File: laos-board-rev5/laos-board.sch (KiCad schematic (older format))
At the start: 98 parts, among them IC1 KB847, IC2 KB847, J1 USB-A, J10 I2C, J11 MBED NXP, J12 JP, J14 ANALOG, J15 JP, J16 JP_3, J17 POLOLU1201, J18 YAXIS, J19 JP, J21 JP, J22 JP_3, J23 POLOLU1201, J24 XAXIS, J25 JP, J27 OUTPUT, J28 VSENSOR, J29 INPUT12, J3 USBPWR, J30 JP, J31 JP_3, J32 POLOLU1201, J33 EAXIS, J34 INPUT34, J35 JP, J37 OUTPUT12, J38 VCPU, J39 OUTPUT34, J4 MAGJACK, J40 JP, J41 O1_SRC, J42 O2_SRC, J43 CONN_4, J5 CONN_3, J6 JP, J7 JP_3, J8 POLOLU1201, J9 ZAXIS, P1 FLATCONN, Q1 TIP115, Q2 TIP115, U1 65HVD251, U2 SDCARD, U3 7805

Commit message: E-axis removed, pololu default 16x microstepping. Fixes #6
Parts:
- removed J30, J35: JP, symbol JP
- removed J31: JP_3, Pkg, symbol JP_3
- removed J32: POLOLU1201, symbol POLOLU1201
- removed J33: EAXIS, Pkg, symbol CONN_5
- removed R11, R14, R20, R6: 1K, symbol R
- removed R13, R16, R25, R9: 10K, symbol R
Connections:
- net labels added: ExhaustEnable, LaserEnable
- net labels removed: E 1A/Step, E 1B/Dir, E 2A/Enable, E 2B/+, EDIR ExhaustEnable, ESTEP LaserEnable
- wire segments 369 -> 385
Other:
- note added: "Microstep setting: 16x. Internal pulldowns in Pololu."
- note removed: "EA/+\nEA/E\nEB/S\nEB/D\nGND"
- note removed: "Microstep setting"
- note removed: "Note: VPP is VMOTOR, bug in kicad power netlist for now ..."
- moved on the sheet: C10, C11, C9, CAN1, D1, IC1, IC2, J12, J15, J16, J17, J18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

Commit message: 'Pololu' means Pololu's A4988 drivers, not the DRV882x drivers. Fixes #6
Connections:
- wire segments 385 -> 403
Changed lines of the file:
@@
-EESchema Schematic File Version 2  date Sun 10 Nov 2013 19:23:53 CET
+EESchema Schematic File Version 2  date Sun 10 Nov 2013 19:41:08 CET
 LIBS:laos_kicad_lib
 LIBS:power
@@
 Comment4 ""
 $EndDescr
+Connection ~ 9400 3350
+Connection ~ 9400 3450
+Connection ~ 9900 3450
+Connection ~ 9900 3350
+Connection ~ 9400 1800
+Connection ~ 9400 1700
+Connection ~ 9900 1700
+Connection ~ 9900 1800
+Wire Wire Line
+	9900 1750 9900 1700
+Wire Wire Line
+	9900 1750 9400 1750
+Wire Wire Line
+	9400 1750 9400 1700
+Wire Wire Line
+	9900 3400 9900 3350
+Wire Wire Line
+	9900 3400 9400 3400
+Wire Wire Line
+	9400 3400 9400 3350
+Wire Wire Line
+	9400 5150 9400 5100
+Wire Wire Line
+	9400 5150 9900 5150
+Wire Wire Line
+	9900 5150 9900 5100
 Wire Wire Line
 	10550 1900 9900 1900
@@
 	14950 5900 14450 5900
 Wire Wire Line
-	3500 3200 3850 3200
-Wire Wire Line
-	3850 3200 4200 3200
+	4200 3200 3850 3200
+Wire Wire Line
+	3850 3200 3500 3200
 Connection ~ 3950 3100
 Wire Wire Line
@@
 	4450 7250 4100 7250
 Wire Wire Line
-	2600 7150 2700 7150
-Wire Wire Line
-	2700 7150 3000 7150
+	3000 7150 2700 7150
+Wire Wire Line
+	2700 7150 2600 7150
 Wire Wire Line
 	11300 5500 13450 5500
@@
 	2700 4850 2450 4850
 Wire Wire Line
-	2150 4400 2450 4400
-Wire Wire Line
-	2450 4400 2875 4400
-Wire Wire Line
-	2875 4400 4200 4400
+	4200 4400 2875 4400
+Wire Wire Line
+	2875 4400 2450 4400
+Wire Wire Line
+	2450 4400 2150 4400
 Wire Wire Line
 	1650 4400 1850 4400
@@
 	6850 1550 6600 1550
 Wire Wire Line
-	3475 10550 3300 10550
-Wire Wire Line
-	3300 10550 3200 10550
+	3200 10550 3300 10550
+Wire Wire Line
+	3300 10550 3475 10550
 Wire Wire Line
 	6100 10100 6100 10300
@@
 Connection ~ 5700 10300
 Wire Wire Line
-	5700 10100 5700 10300
-Wire Wire Line
-	5700 10300 5700 10400
+	5700 10400 5700 10300
+Wire Wire Line
+	5700 10300 5700 10100
 Wire Wire Line
 	11300 2300 11550 2300
 Wire Wire Line
-	9900 1800 10550 1800
+	10550 1800 9900 1800
 Wire Wire Line
 	13250 2600 13250 2675
@@
 	13450 2000 11300 2000
 Wire Wire Line
-	11300 1800 13250 1800
-Wire Wire Line
-	13250 1800 13450 1800
+	13450 1800 13250 1800
+Wire Wire Line
+	13250 1800 11300 1800
 Connection ~ 9350 1800
 Wire Wire Line
-	9350 1700 9400 1700
+	9400 1700 9350 1700
 Wire Wire Line
 	10450 2100 10450 2000
@@
 	11400 1500 11400 2200
 Wire Wire Line
-	9400 1800 9350 1800
+	9350 1800 9400 1800
 Connection ~ 9350 1700
 Wire Wire Line
@@
 Connection ~ 9350 3450
 Wire Wire Line
-	11300 3450 13250 3450
-Wire Wire Line
-	13250 3450 13450 3450
+	13450 3450 13250 3450
+Wire Wire Line
+	13250 3450 11300 3450
 Connection ~ 13250 3450
 Wire Wire Line
 	13250 4325 13250 4250
 Wire Wire Line
-	9900 3450 10550 3450
+	10550 3450 9900 3450
 Wire Wire Line
 	11300 3950 11550 3950
@@
 	11300 5700 11550 5700
 Wire Wire Line
-	9900 5200 10550 5200
+	10550 5200 9900 5200
 Wire Wire Line
 	13250 6075 13250 6000
@@
 Connection ~ 9350 5200
 Wire Wire Line
-	9350 5100 9400 5100
+	9400 5100 9350 5100
 Wire Wire Line
 	10450 5500 10450 5400
@@
 	11400 4900 11400 5600
 Wire Wire Line
-	9400 5200 9350 5200
+	9350 5200 9400 5200
 Connection ~ 9350 5100
 Wire Wire Line
@@
 	1650 10650 1650 10950
 Wire Wire Line
-	2800 10850 2800 10950
-Wire Wire Line
-	2800 10950 2800 10975
+	2800 10975 2800 10950
+Wire Wire Line
+	2800 10950 2800 10850
 Wire Wire Line
 	5400 1200 5400 1300
@@
 Connection ~ 1625 825
 Wire Wire Line
-	1625 775  1625 825
-Wire Wire Line
-	1625 825  1625 1025
+	1625 1025 1625 825
+Wire Wire Line
+	1625 825  1625 775
 Wire Wire Line
 	1775 825  1625 825
@@
 	1625 825  1475 825
 Wire Wire Line
-	5400 750  5400 770
-Wire Wire Line
-	5400 770  5400 800
+	5400 800  5400 770
+Wire Wire Line
+	5400 770  5400 750
 Wire Wire Line
 	1475 825  1475 1025
@@
 	1800 7150 1800 7450
 Wire Wire Line
-	2450 4450 2450 4400
-Wire Wire Line
-	2450 4400 2450 4200
+	2450 4200 2450 4400
+Wire Wire Line
+	2450 4400 2450 4450
 Wire Wire Line
 	4750 8900 4750 8900
@@
 	1850 1750 1850 1800
 Wire Wire Line
-	7100 4150 6700 4150
-Wire Wire Line
-	6700 4150 6600 4150
+	6600 4150 6700 4150
+Wire Wire Line
+	6700 4150 7100 4150
 Wire Wire Line
 	6600 3850 7100 3850
@@
 	2450 4850 2450 4750
 Wire Wire Line
-	2875 4400 2875 4425
+	2875 4425 2875 4400
 Connection ~ 2875 4400
 Wire Wire Line
@@
 	13750 5400 13750 5500
 Wire Wire Line
-	3000 7250 2800 7250
-Wire Wire Line
-	2800 7250 2600 7250
-Wire Wire Line
-	5050 7650 5200 7650
-Wire Wire Line
-	5200 7650 5300 7650
+	2600 7250 2800 7250
+Wire Wire Line
+	2800 7250 3000 7250
+Wire Wire Line
+	5300 7650 5200 7650
+Wire Wire Line
+	5200 7650 5050 7650
 Connection ~ 5200 7650
 Wire Wire Line
@@
 Connection ~ 3850 3200
 Wire Wire Line
-	3500 3100 3950 3100
-Wire Wire Line
-	3950 3100 4200 3100
+	4200 3100 3950 3100
+Wire Wire Line
+	3950 3100 3500 3100
 Wire Wire Line
 	2550 9000 2150 9000
@@
 Wire Wire Line
 	9900 2000 9900 1900
+Wire Wire Line
+	9400 5200 9400 5250
+Wire Wire Line
+	9400 5250 9900 5250
+Wire Wire Line
+	9900 5250 9900 5200
+Connection ~ 9900 5200
+Connection ~ 9400 5200
+Connection ~ 9400 5100
+Connection ~ 9900 5100
+Wire Wire Line
+	9900 3450 9900 3500
+Wire Wire Line
+	9900 3500 9400 3500
+Wire Wire Line
+	9400 3500 9400 3450
+Wire Wire Line
+	9900 1800 9900 1850
+Wire Wire Line
+	9900 1850 9400 1850
+Wire Wire Line
+	9400 1850 9400 1800
 $Comp
 L VMOT #PWR?

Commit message: First functional version, TODO: some polishing and refining
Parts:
- removed J38: VCPU, Pkg, symbol CONN_2
- C1, C3, C5, C7, C8: footprint Pkg -> C_CER
- C10, C11, C9: footprint Pkg -> C1V7HF
- C4: footprint Pkg -> CCAP_5MM
- C6: footprint Pkg -> CCAP_3.5MM
- CAN1: value RJ12 -> Molex 95501-2641; footprint (none) -> RJ12_MOLEX_95501-2641; Manufacturer (none) -> Molex; Type (none) -> 95501-2641
- D1, D2, D3: footprint (none) -> LED-3MM
- H1, H2, H3, H4: footprint (none) -> HOLE_3MM
- IC1, IC2: footprint DIP16 -> 16DIP300-ELL
- J10, J14, J27, J29, J34, J37, J39: footprint Pkg -> CONN_4
- J11: footprint (none) -> MBED
- J12, J15, J19, J21, J25, J3, J6: footprint (none) -> SJ
- J16, J22, J7: footprint Pkg -> SJ_3
- J17, J23, J8: footprint (none) -> POLOLU1201
- J18, J24, J9: footprint Pkg -> CONN_5
- J28, J41, J42: footprint (none) -> SIL-3
- J4: footprint (none) -> RJ45_HALO_HFJ11
- J40: footprint (none) -> SIL-2
- J43: footprint Pkg -> SIL-4a
- J5: footprint (none) -> CONN_3
- P1: footprint (none) -> FLAT-12
- Q1, Q2: value TIP115 -> TIP110; footprint T220-3 -> TO220V-BCE
- R1, R10, R12, R15, R17, R18, R19, R2, R21, R22, R23, R24, R26, R27, R28, R29, R3, R30, R31, R32, R4, R5, R7, R8: footprint (none) -> R4
- R33, R34: footprint Pkg -> R4
- U1: footprint (none) -> 8DIP300-ELL
- U2: footprint (none) -> HIROSE_DM1B-DSF-PEJ
- U3: footprint (none) -> TO220V-123
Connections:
- net labels added: +5V USB, RX+, RX-, TX+, TX-, VCPU
- net labels removed: VAA
- wire segments 403 -> 356
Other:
- note added: "1-2: VCPU\n2-3: VMOT"
- note added: "VCPU\nGND\nVMOT"
- note added: "Vsensor jumper"
- note removed: "1-2: 5V\n2-3: VMOT"
- note removed: "VCPU\nGND"
- note removed: "VMOT\nGND\nVAA"
- moved on the sheet: C3, C4, C6, C7, C8, CAN1, D2, D3, IC1, IC2, J1, J29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

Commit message: Last changes and small improvenments
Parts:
- removed J15, J21, J6: JP, SJ, symbol JP
- added C2: 100nF, C_CER, symbol C
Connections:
- wire segments 356 -> 358
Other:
- moved on the sheet: CAN1, R1, U1

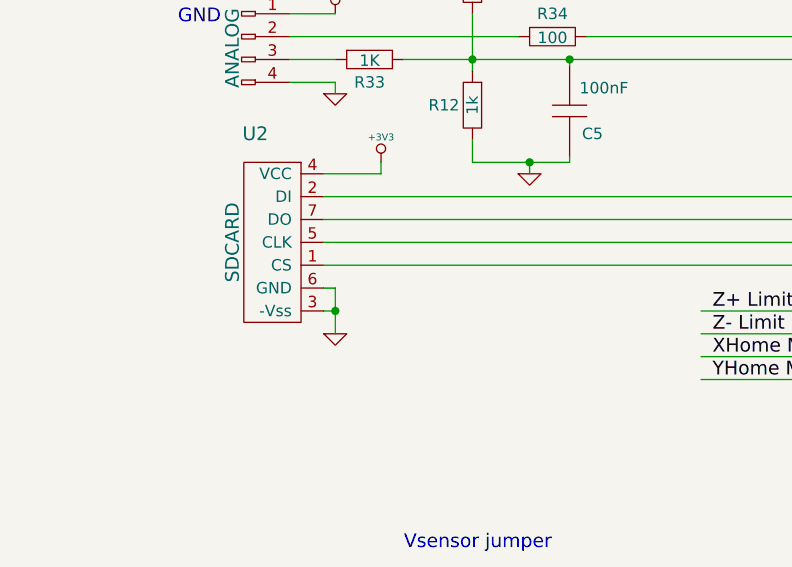
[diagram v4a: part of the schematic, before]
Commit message: Micro SD card holder
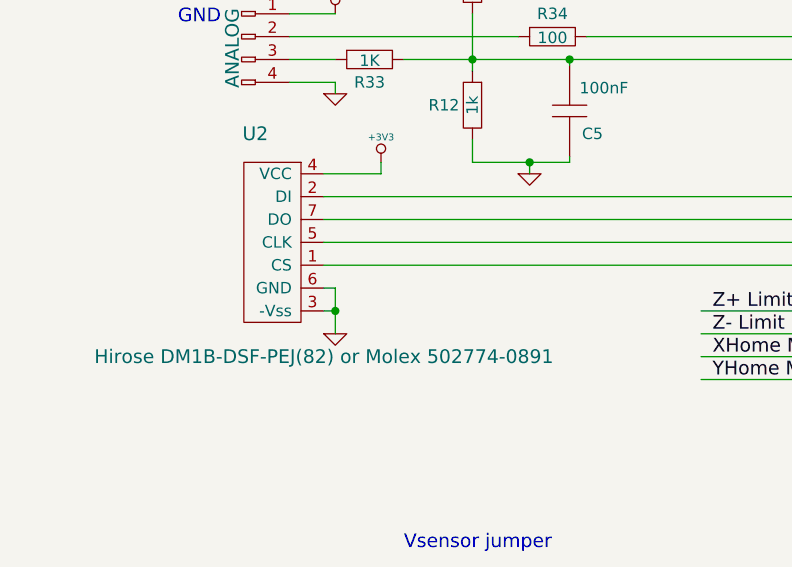
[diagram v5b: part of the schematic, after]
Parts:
- H2: footprint HOLE_3MM -> HOLE_3MM_OVAL
- J28, J41, J42: footprint SIL-3 -> SIL-3-noarrow
- U2: value SDCARD -> Hirose DM1B-DSF-PEJ(82) or Molex 502774-0891; footprint HIROSE_DM1B-DSF-PEJ -> HIROSE_DM1B-DSF-PEJ_MOLEX_502774-0891; Manufacturer (none) -> Hirose/Molex; Type (none) -> DM1B-DSF-PEJ(82)/502774-0891
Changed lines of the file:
@@
-EESchema Schematic File Version 2  date Wed 01 Jan 2014 04:18:42 PM CET
+EESchema Schematic File Version 2  date Thu 02 Jan 2014 12:04:35 PM CET
 LIBS:laos_kicad_lib
 LIBS:power
@@
 Sheet 1 1
 Title "LaOS Laser Mainboard"
-Date "1 jan 2014"
+Date "2 jan 2014"
 Rev "5"
 Comp "http://www.laoslaser.org"
@@
 F 0 "J42" V 12040 9950 60  0000 C CNN
 F 1 "O2_SRC" H 12100 9700 60  0000 C CNN
-F 2 "SIL-3" H 12100 9800 60  0001 C CNN
+F 2 "SIL-3-noarrow" H 12100 9800 60  0001 C CNN
 	1    12100 9800
 	0    1    1    0
@@
 F 0 "J41" V 12040 9300 60  0000 C CNN
 F 1 "O1_SRC" H 12100 9050 60  0000 C CNN
-F 2 "SIL-3" H 12100 9150 60  0001 C CNN
+F 2 "SIL-3-noarrow" H 12100 9150 60  0001 C CNN
 	1    12100 9150
 	0    1    1    0
@@
 F 0 "H2" H 15550 800 60  0000 C CNN
 F 1 "MOUNT_HOLE" H 15600 1100 60  0001 C CNN
-F 2 "HOLE_3MM" H 15600 1200 60  0001 C CNN
+F 2 "HOLE_3MM_OVAL" H 15600 1200 60  0001 C CNN
 	1    15600 850
 	1    0    0    -1
@@
 F 0 "J28" V 13440 8850 60  0000 C CNN
 F 1 "VSENSOR" H 13500 8600 60  0000 C CNN
-F 2 "SIL-3" H 13500 8700 60  0001 C CNN
+F 2 "SIL-3-noarrow" H 13500 8700 60  0001 C CNN
 	1    13500 8700
 	-1   0    0    1
@@
 P 1550 5100
 F 0 "U2" H 1500 5475 60  0000 C CNN
-F 1 "SDCARD" V 1400 5000 60  0000 C CNN
-F 2 "HIROSE_DM1B-DSF-PEJ" V 1500 5000 60  0001 C CNN
+F 1 "Hirose DM1B-DSF-PEJ(82) or Molex 502774-0891" H 1800 4500 60  0000 C CNN
+F 2 "HIROSE_DM1B-DSF-PEJ_MOLEX_502774-0891" V 1500 5000 60  0001 C CNN
+F 4 "Hirose/Molex" H 1550 5100 60  0001 C CNN "Manufacturer"
+F 5 "DM1B-DSF-PEJ(82)/502774-0891" H 1550 5100 60  0001 C CNN "Type"
 	1    1550 5100
 	1    0    0    -1

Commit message: Sikscreen texts on back side, output files generated
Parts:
- IC1: Farnell (none) -> 2001656; RS (none) -> 619-2026
- J11: Farnell (none) -> 1761179; RS (none) -> 703-9238
- J17, J23, J8: value POLOLU1201 -> Pololu 1182 (A4988); Other (none) -> Pololu 1182
- J4: Farnell (none) -> 1137981; Manufacturer (none) -> MAGJACK; RS (none) -> 741-8477; Type (none) -> SI-60002-F
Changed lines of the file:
@@
-EESchema Schematic File Version 2  date Thu 02 Jan 2014 12:04:35 PM CET
+EESchema Schematic File Version 2  date Fri 03 Jan 2014 10:11:41 AM CET
 LIBS:laos_kicad_lib
 LIBS:power
@@
 Sheet 1 1
 Title "LaOS Laser Mainboard"
-Date "2 jan 2014"
+Date "3 jan 2014"
 Rev "5"
 Comp "http://www.laoslaser.org"
@@
 F 1 "MBED NXP" H 5450 4200 60  0000 C CNN
 F 2 "MBED" H 5450 4300 60  0001 C CNN
+F 4 "1761179" H 5400 3400 60  0001 C CNN "Farnell"
+F 5 "703-9238" H 5400 3400 60  0001 C CNN "RS"
 	1    5400 3400
 	1    0    0    -1
@@
 P 10900 2000
 F 0 "J8" H 10700 1525 60  0000 C CNN
-F 1 "POLOLU1201" H 10925 2550 60  0000 C CNN
+F 1 "Pololu 1182 (A4988)" H 10850 2550 60  0000 C CNN
 F 2 "POLOLU1201" H 10925 2650 60  0001 C CNN
+F 4 "Pololu 1182" H 10900 2000 60  0001 C CNN "Other"
 	1    10900 2000
 	1    0    0    -1
@@
 P 10900 3650
 F 0 "J17" H 10700 3175 60  0000 C CNN
-F 1 "POLOLU1201" H 10925 4200 60  0000 C CNN
+F 1 "Pololu 1182 (A4988)" H 10850 4200 60  0000 C CNN
 F 2 "POLOLU1201" H 10925 4300 60  0001 C CNN
+F 4 "Pololu 1182" H 10900 3650 60  0001 C CNN "Other"
 	1    10900 3650
 	1    0    0    -1
@@
 P 10900 5400
 F 0 "J23" H 10700 4925 60  0000 C CNN
-F 1 "POLOLU1201" H 10925 5950 60  0000 C CNN
+F 1 "Pololu 1182 (A4988)" H 10850 5950 60  0000 C CNN
 F 2 "POLOLU1201" H 10925 6050 60  0001 C CNN
+F 4 "Pololu 1182" H 10900 5400 60  0001 C CNN "Other"
 	1    10900 5400
 	1    0    0    -1
@@
 F 1 "KB847" H 4800 8925 50  0000 L BNN
 F 2 "16DIP300-ELL" H 5050 7550 50  0001 C CNN
+F 4 "2001656" H 5050 8250 60  0001 C CNN "Farnell"
+F 5 "619-2026" H 5050 8250 60  0001 C CNN "RS"
 	1    5050 8250
 	1    0    0    -1
@@
 F 1 "MAGJACK" V 1350 1850 60  0000 C CNN
 F 2 "RJ45_HALO_HFJ11" V 1450 1850 60  0001 C CNN
+F 4 "MAGJACK" H 1550 2000 60  0001 C CNN "Manufacturer"
+F 5 "SI-60002-F" H 1550 2000 60  0001 C CNN "Type"
+F 6 "1137981" H 1550 2000 60  0001 C CNN "Farnell"
+F 7 "741-8477" H 1550 2000 60  0001 C CNN "RS"
 	1    1550 2000
 	1    0    0    -1
